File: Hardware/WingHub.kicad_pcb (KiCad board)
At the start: 2 copper layers, 50.8 x 22.9 mm, 15 parts, among them J1 Conn_Battery, J2 USB_A, J3 USB_A, J4 USB_B_Micro, J5 Conn_Left, J6 Conn_Right, SW1 RESET, SW2 DOWLOADER, U1 CH559L

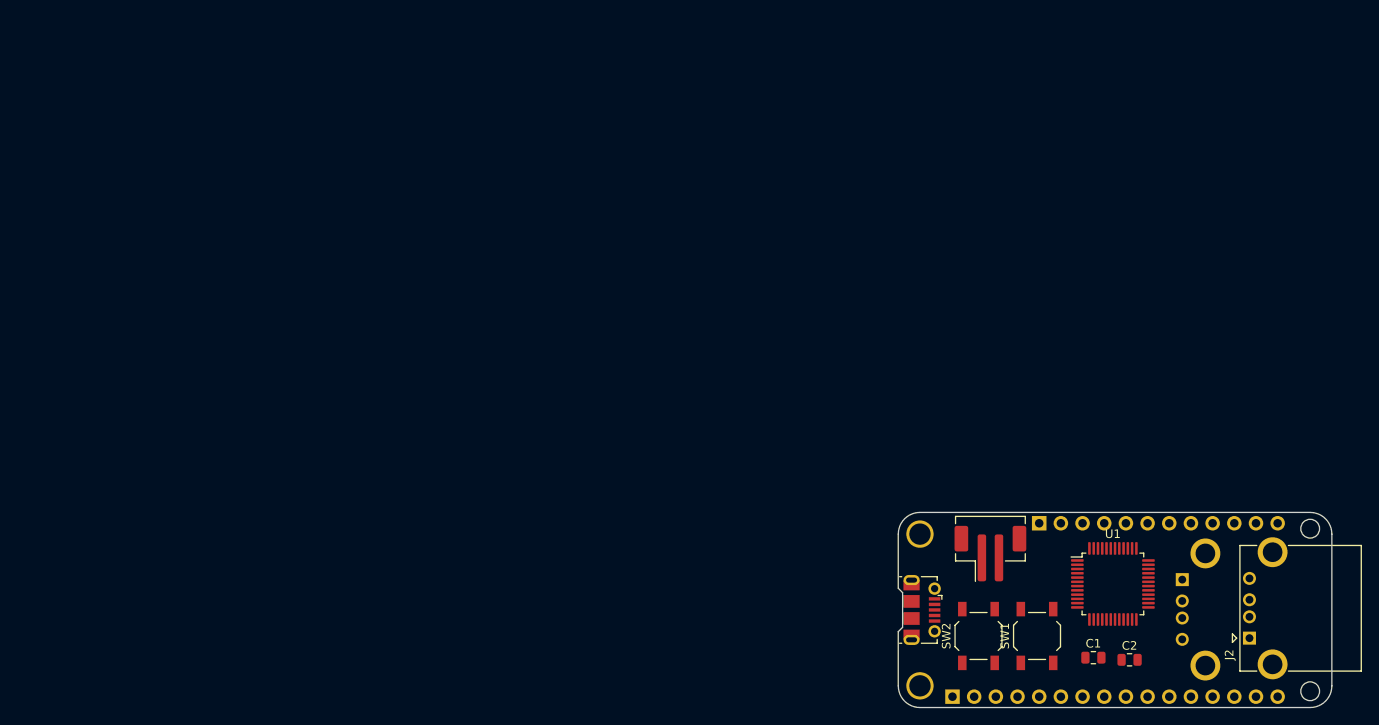
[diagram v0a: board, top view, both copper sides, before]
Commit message: Update Wings format
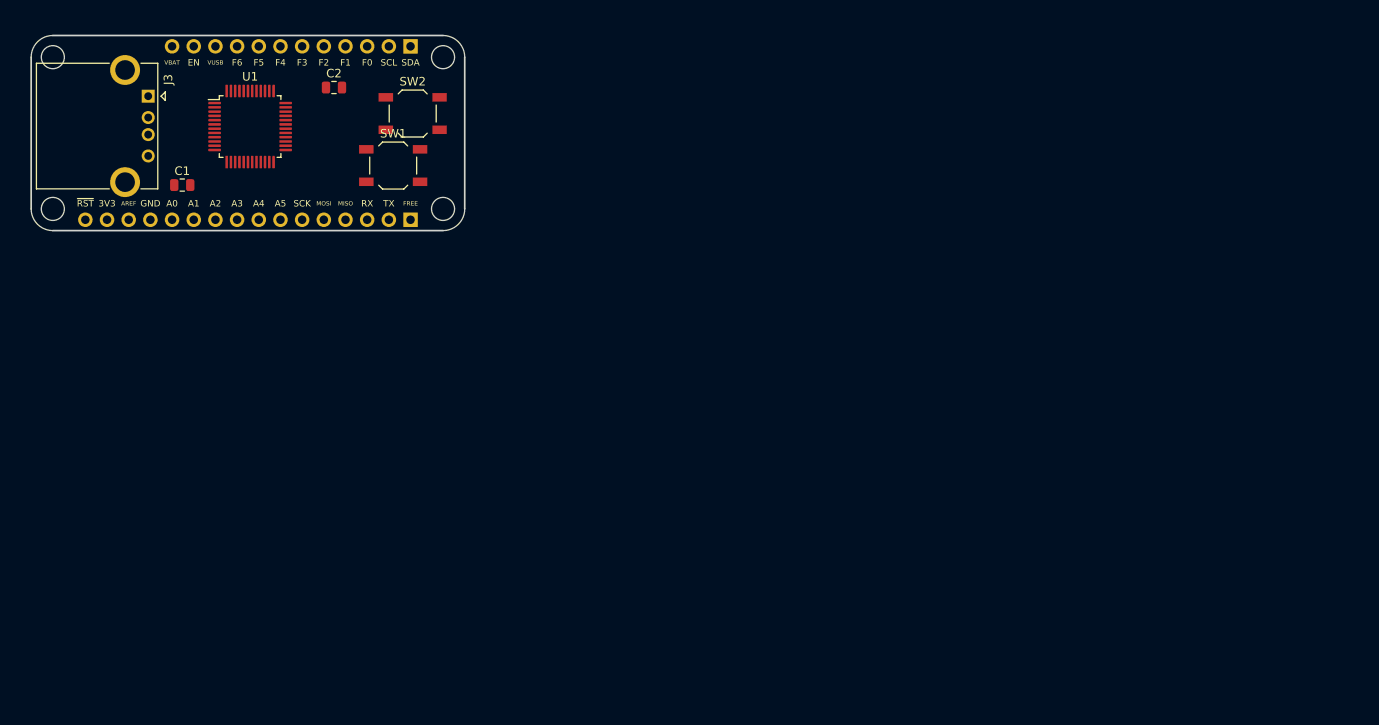
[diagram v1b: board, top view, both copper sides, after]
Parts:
- removed J4: USB_B_Micro, Connector_USB:USB_Micro-B_Molex-105017-0001
- removed J5: Conn_Left, Connector_PinSocket_2.54mm:PinSocket_1x16_P2.54mm_Vertical
- removed J6: Conn_Right, Connector_PinSocket_2.54mm:PinSocket_1x12_P2.54mm_Vertical
- removed the REF** at (129.5, 83.8)
- removed the REF** at (129.5, 101.6)
- removed the REF** at (175.3, 102.2)
- removed the REF** at (175.3, 83.2)
- added REF**: MountingHole_2.7mm_M2.5, MountingHole:MountingHole_2.7mm_M2.5, F.Cu at (73.7, 27.9)
- added REF**: MountingHole_2.7mm_M2.5, MountingHole:MountingHole_2.7mm_M2.5, F.Cu at (73.7, 45.7)
- added REF**: MountingHole_2.7mm_M2.5, MountingHole:MountingHole_2.7mm_M2.5, F.Cu at (27.9, 45.7)
- added REF**: MountingHole_2.7mm_M2.5, MountingHole:MountingHole_2.7mm_M2.5, F.Cu at (27.9, 27.9)
- J1: value Conn_Battery -> feather long; footprint Connector_JST:JST_PH_B2B-PH-SM4-TB_1x02-1MP_P2.00mm_Vertical -> Connector_PinHeader_2.54mm:PinHeader_1x16_P2.54mm_Vertical; moved to B.Cu
- J2: value USB_A -> feather short; footprint Connector_USB:USB_A_CONNFLY_DS1095-WNR0 -> Connector_PinHeader_2.54mm:PinHeader_1x12_P2.54mm_Vertical; moved to B.Cu
- J3: moved to F.Cu
- moved J3 133.7 mm to (39.1, 32.5)
- moved J2 120.3 mm to (69.8, 26.7)
- moved C1 120.3 mm to (43.1, 42.9)
- moved C2 114.8 mm to (60.9, 31.5)
- moved U1 114.4 mm to (51.1, 36.1)
- moved SW1 93.4 mm to (67.8, 40.6), turned to 0 degrees
- moved SW2 90.2 mm to (70.1, 34.5), turned to 0 degrees
- moved J1 78.4 mm to (69.8, 47.0), turned to 90 degrees
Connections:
- net Net-(J2-Pad5) renamed /F2
- J1 pad 1: GND -> /FREE
- J1 pad 2: +BATT -> /TX
- J2 pad 1: VBUS -> /SDA
- J2 pad 2: /D2- -> /SCL
- J2 pad 3: /D2+ -> /F0
- J2 pad 4: GND -> /F1
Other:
- outline, holes or cut-outs redrawn
- board text added: "3V3"
- board text added: "A0"
- board text added: "A1"
- board text added: "A2"
- board text added: "A3"
- board text added: "A4"
- board text added: "A5"
- board text added: "AREF"
- board text added: "EN"
- board text added: "F0"
- board text added: "F1"
- board text added: "F2"
- board text added: "F3"
- board text added: "F4"
- board text added: "F5"
- board text added: "F6"
- board text added: "FREE"
- board text added: "GND"
- board text added: "MISO"
- board text added: "MOSI"
- board text added: "RX"
- board text added: "SCK"
- board text added: "SCL"
- board text added: "SDA"
- board text added: "TX"
- board text added: "VBAT"
- board text added: "VUSB"
- board text added: "~RST"

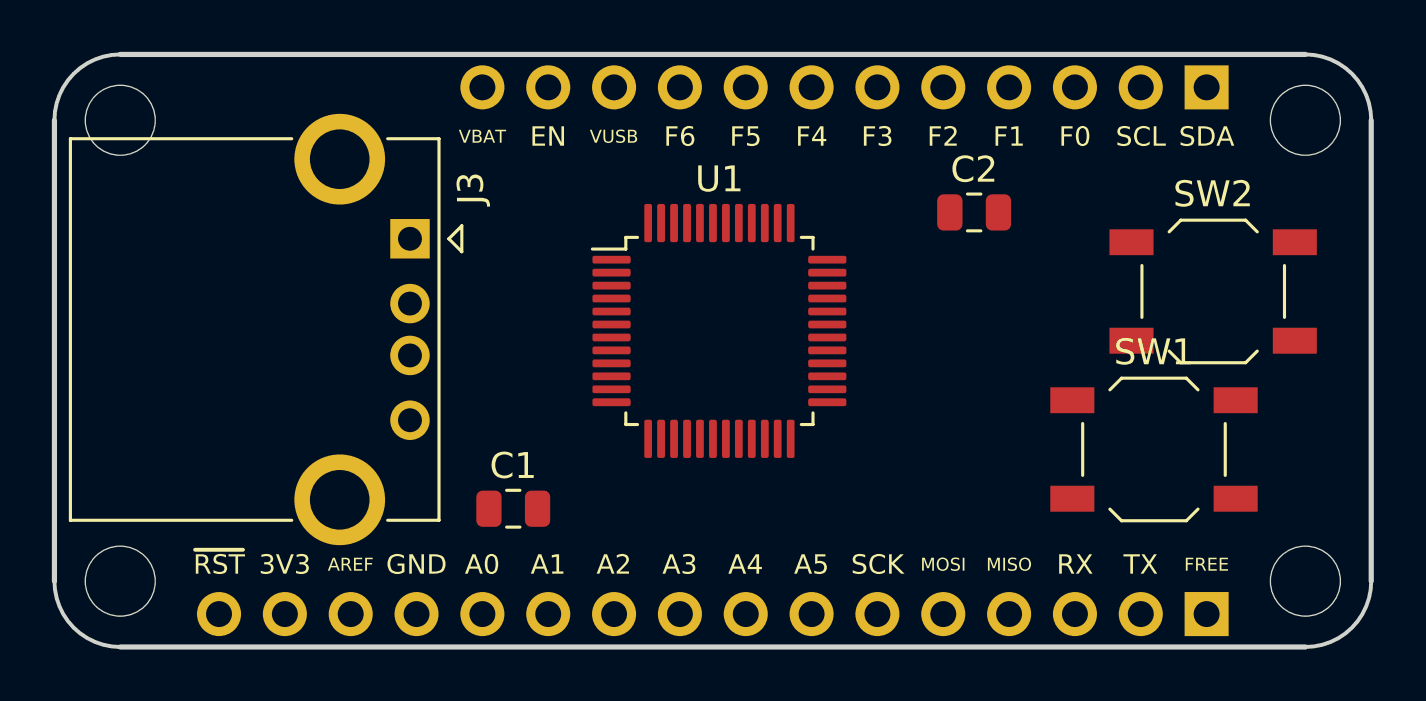
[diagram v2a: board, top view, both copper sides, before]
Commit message: Pre-routed HUSUSB PCB
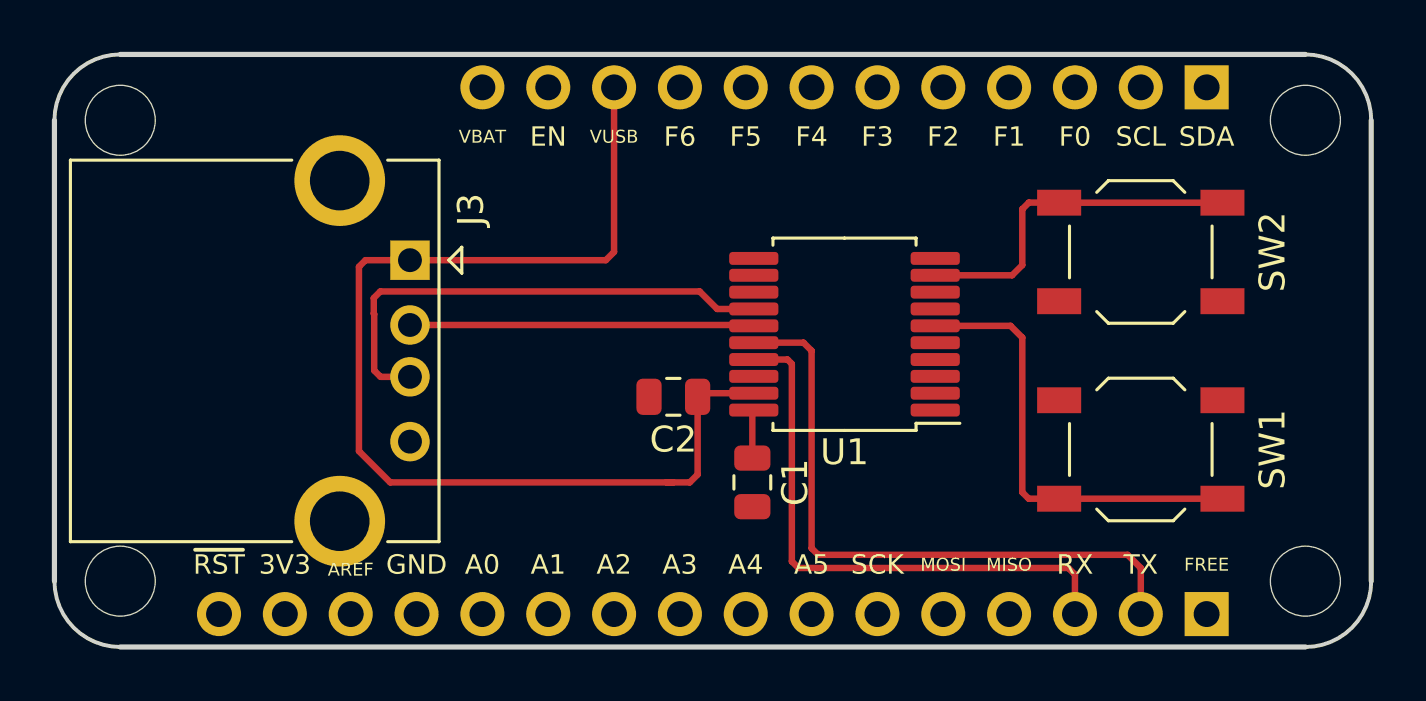
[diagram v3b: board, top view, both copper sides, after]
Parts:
- SW2: value DOWLOADER -> DOWNLOADER
- U1: value CH559L -> CH559T; footprint Package_QFP:LQFP-48_7x7mm_P0.5mm -> Package_SO:SSOP-20_5.3x7.2mm_P0.65mm
- moved C2 13.6 mm to (49.3, 38.6), turned to 180 degrees
- moved C1 9.28 mm to (52.3, 41.9), turned to 270 degrees
- moved U1 4.83 mm to (55.9, 36.2), turned to 180 degrees
- moved SW2 3.18 mm to (67.3, 33.0)
- moved J3 0.83 mm to (39.1, 33.3)
- moved SW1 0.51 mm to (67.3, 40.6), turned to 180 degrees
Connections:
- net /A0 renamed Net-(J1-Pad12)
- net /A1 renamed Net-(J1-Pad11)
- net /A2 renamed Net-(J1-Pad10)
- net /A3 renamed Net-(J1-Pad9)
- net /A4 renamed Net-(J1-Pad8)
- net /A5 renamed Net-(J1-Pad7)
- net /AREF renamed Net-(J1-Pad14)
- net /EN renamed Net-(J2-Pad11)
- net /F0 renamed Net-(J2-Pad3)
- net /F1 renamed Net-(J2-Pad4)
- net /F2 renamed Net-(J2-Pad5)
- net /F3 renamed Net-(J2-Pad6)
- net /F4 renamed Net-(J2-Pad7)
- net /F5 renamed Net-(J2-Pad8)
- net /F6 renamed Net-(J2-Pad9)
- net /FREE renamed Net-(J1-Pad1)
- net /MISO renamed Net-(J1-Pad4)
- net /MOSI renamed Net-(J1-Pad5)
- net /SCK renamed Net-(J1-Pad6)
- net /SCL renamed Net-(J2-Pad2)
- net /SDA renamed Net-(J2-Pad1)
- net /VBAT renamed Net-(J2-Pad12)
- C1 pad 1: VBUS -> +3V3
- C2 pad 1: +3V3 -> VBUS
- J1 pad 16: /~RST -> /RST
- J2 pad 10: /VUSB -> VBUS
- J3 pad 2: /D1- -> /D-
- J3 pad 3: /D1+ -> /D+
- SW1 pad 1: GND -> /RST
- SW1 pad 2: /RST -> GND
- SW2 pad 1: GND -> /PROG
- SW2 pad 2: /PROG -> GND
- U1 pad 14: Net-(U1-Pad14) -> /D+
- U1 pad 15: Net-(U1-Pad15) -> /D-
- U1 pad 16: /PROG -> /TX
- U1 pad 17: Net-(U1-Pad17) -> /RX
- U1 pad 19: Net-(U1-Pad19) -> VBUS
- U1 pad 20: Net-(U1-Pad20) -> +3V3
- U1 pad 3: /RST -> Net-(U1-Pad3)
- U1 pad 6: Net-(U1-Pad6) -> /RST
- U1 pad 9: Net-(U1-Pad9) -> /PROG
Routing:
- net VBUS: track 0.00 -> 42.7 mm
- net /TX: track 0.00 -> 24.8 mm
- net /RX: track 0.00 -> 21.8 mm
- net /D+: track 0.00 -> 19.3 mm
- net /RST: track 0.00 -> 17.3 mm
- net /PROG: track 0.00 -> 13.5 mm
- net /D-: track 0.00 -> 13.3 mm
- net +3V3: track 0.00 -> 1.88 mm

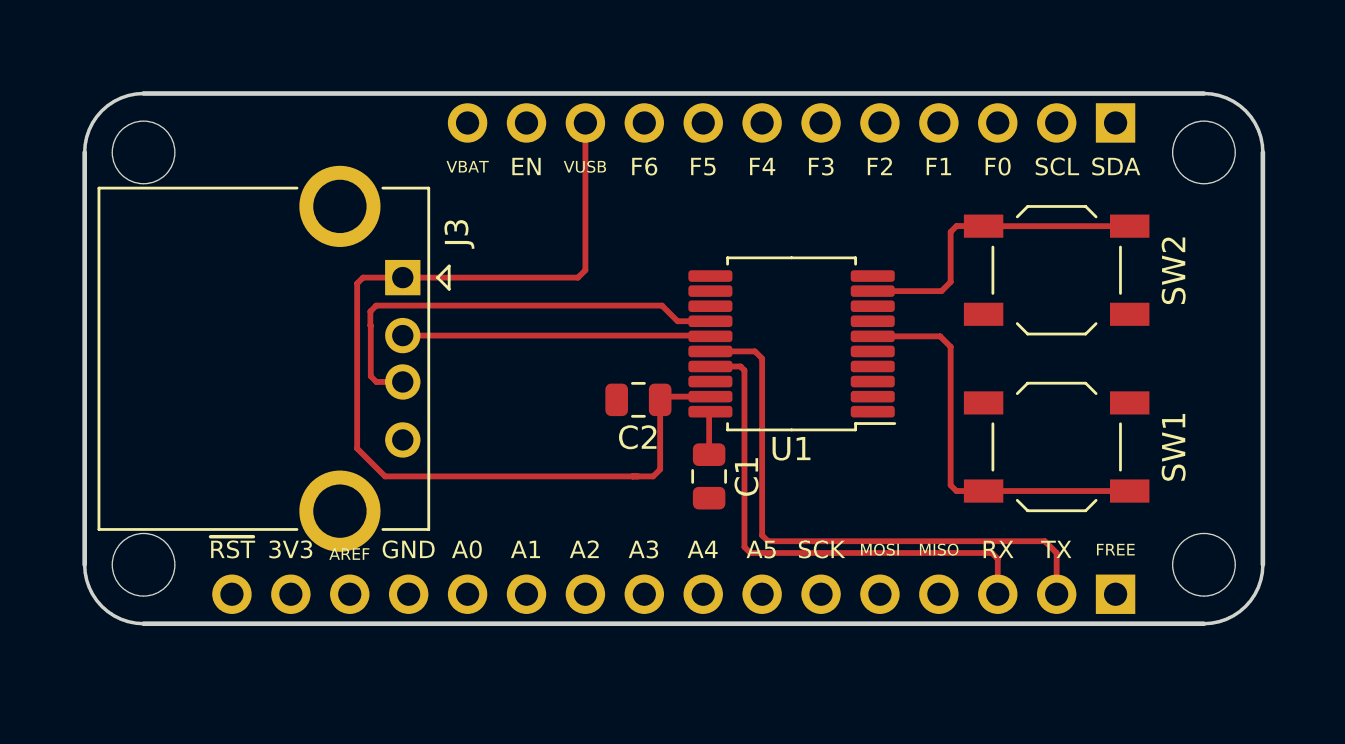
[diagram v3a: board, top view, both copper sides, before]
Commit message: Routed and copper-zone-filled HUSUSB_PCB
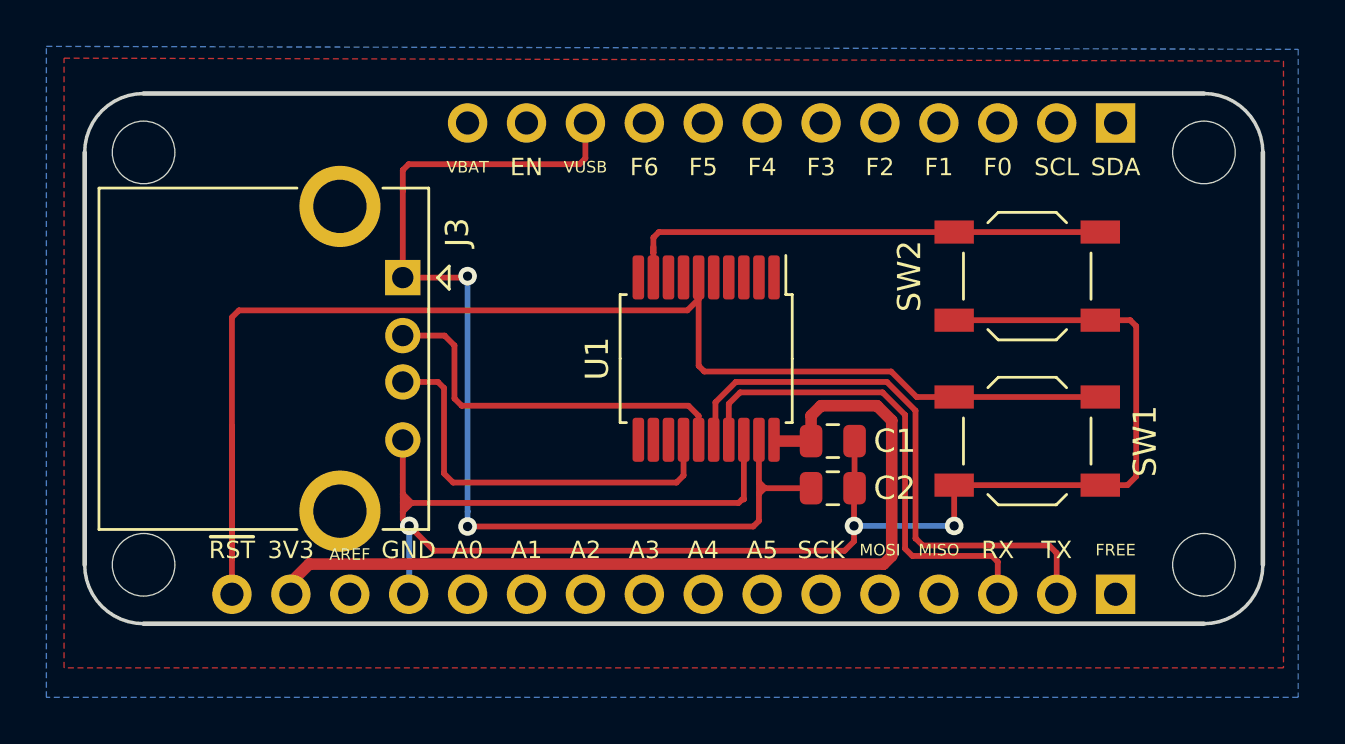
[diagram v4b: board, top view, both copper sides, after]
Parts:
- moved C2 9.21 mm to (57.7, 42.4), turned to 0 degrees
- moved C1 5.55 mm to (57.7, 40.4), turned to 0 degrees
- moved U1 3.74 mm to (52.2, 36.8), turned to 270 degrees
- moved SW1 1.30 mm to (66.0, 40.4), turned to 0 degrees
- moved SW2 1.30 mm to (66.0, 33.3)
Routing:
- net GND: track 0.00 -> 79.2 mm, vias 0 -> 3
- net /RST: track 17.3 -> 59.8 mm
- net +3V3: track 1.88 -> 39.4 mm
- net /PROG: track 13.5 -> 21.3 mm
- net VBUS: track 42.7 -> 47.3 mm, vias 0 -> 2
- net /D-: track 13.3 -> 16.6 mm
- net /D+: track 19.3 -> 17.7 mm
- net /RX: track 21.8 -> 21.2 mm
- added copper zone on B.Cu, net GND
- added copper zone on F.Cu, net GND
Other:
- net class Voltage added: clearance 0.2, trace_width 0.5, via_dia 0.8, via_drill 0.4

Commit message: add logos and LED serial data
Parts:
- added D1: LED, LED_SMD:LED_0805_2012Metric, F.Cu at (46.0, 35.6)
- added G***: LOGO, Aesthetics:electronic_cats_logo_4x3, F.Cu at (45.0, 41.4)
- added G***: LOGO, Aesthetics:electronic_cats_logo_8x6, B.Cu at (69.6, 37.1)
- added R1: 1K, Resistor_SMD:R_0805_2012Metric, F.Cu at (45.9, 31.1)
- added REF**: OSHW-Logo_7.5x8mm_SilkScreen, Symbol:OSHW-Logo_7.5x8mm_SilkScreen, B.Cu at (32.5, 36.6)
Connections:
- J1 pad 16: /RST -> Net-(J1-Pad16)
- J1 pad 4: Net-(J1-Pad4) -> /MISO
- J1 pad 5: Net-(J1-Pad5) -> /MOSI
- J1 pad 6: Net-(J1-Pad6) -> /SCK
- J2 pad 6: Net-(J2-Pad6) -> /CS
- U1 pad 2: Net-(U1-Pad2) -> /CS
- U1 pad 3: Net-(U1-Pad3) -> /MOSI
- U1 pad 4: Net-(U1-Pad4) -> /MISO
- U1 pad 5: Net-(U1-Pad5) -> /SCK
- U1 pad 7: Net-(U1-Pad7) -> /LED
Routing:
- net /RST: track 59.8 -> 20.4 mm
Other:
- board text added: "FeatherWings HubUSB CH559"
- board text removed: "3V3"
- board text removed: "A0"
- board text removed: "A1"
- board text removed: "A2"
- board text removed: "A3"
- board text removed: "EN"
- board text removed: "F0"
- board text removed: "F1"
- board text removed: "F2"
- board text removed: "F3"
- board text removed: "F4"
- board text removed: "F5"
- board text removed: "F6"
- board text removed: "SCL"
- board text removed: "SDA"
- board text removed: "VBAT"
- board text removed: "~RST"
